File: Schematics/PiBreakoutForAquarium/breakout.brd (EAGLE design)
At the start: 57.1 x 87.3 mm, 17 parts, among them U1 MSP430G2402IN20

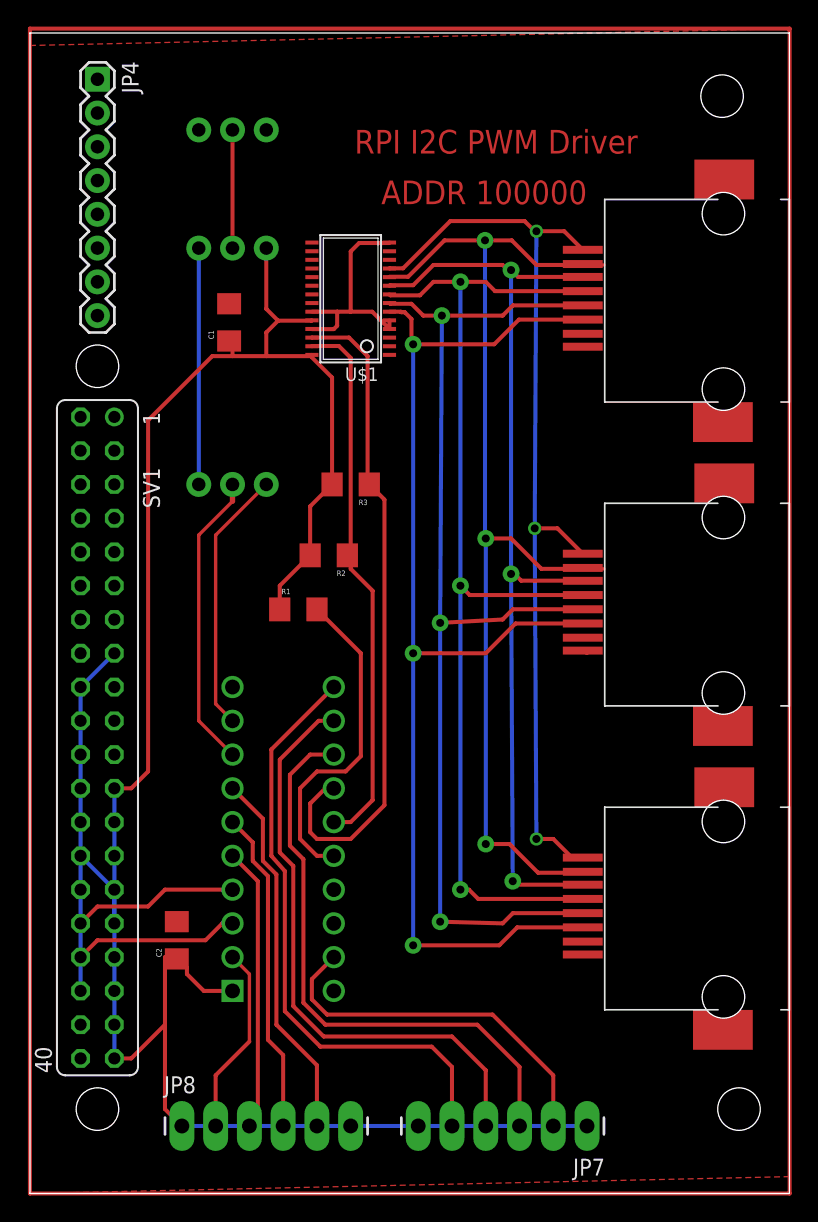
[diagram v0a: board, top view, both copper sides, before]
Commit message: New AVR based firmware
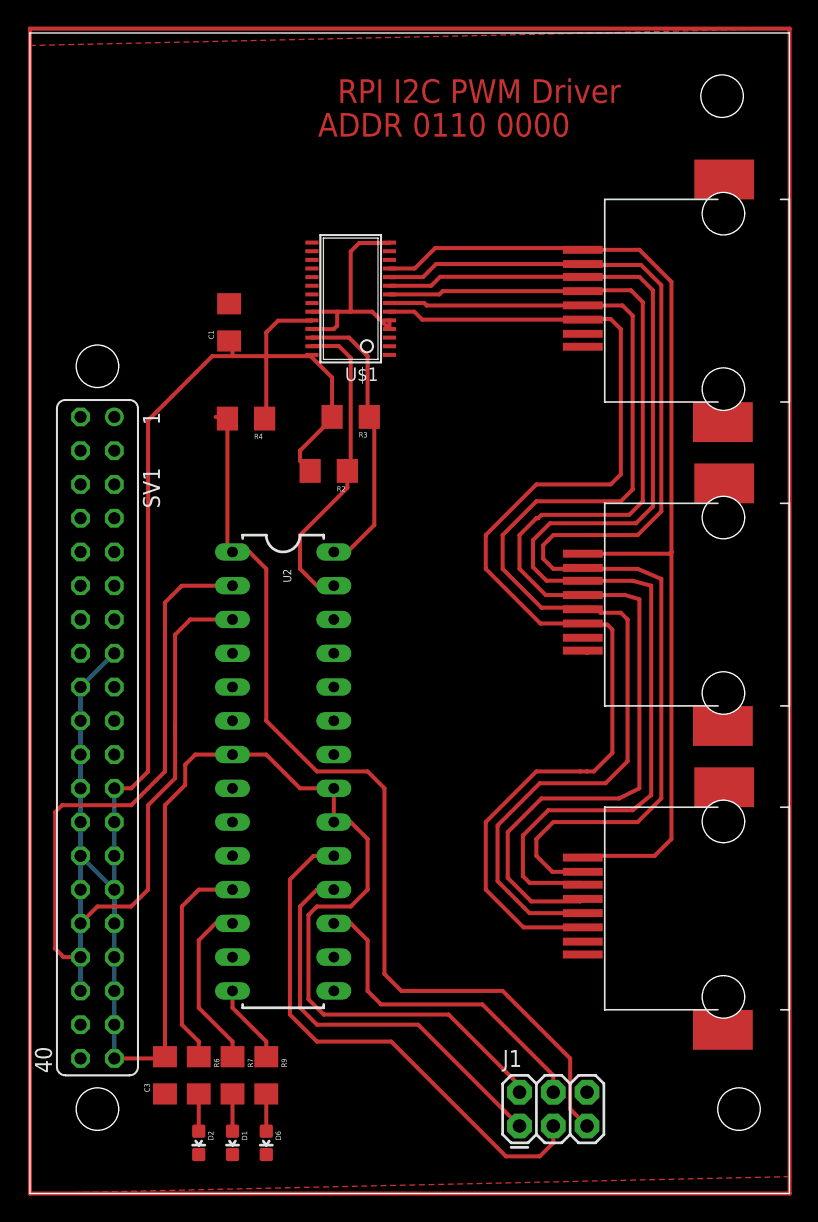
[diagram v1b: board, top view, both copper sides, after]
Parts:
- removed C2: .1 uF, SparkFun-Capacitors:1206
- removed JP2, JP3, JP5: (no value), SparkFun-Connectors:1X03
- removed JP4: (no value), SparkFun-Connectors:1X08
- removed JP7, JP8: (no value), SparkFun-Connectors:1X06_LONGPADS
- removed R1: 47K, SparkFun-Resistors:1206
- removed U1: MSP430G2402IN20, Texas Instruments_By_element14_Batch_1:DIP254P762X508-20
- added C3: (no value), SparkFun-Capacitors:1206
- added D1, D2, D6: (no value), SparkFun-LED:LED-0603
- added J1: FEMALE 2x3, SparkFun-Connectors:2X3
- added R4, R6, R7, R9: (no value), SparkFun-Resistors:1206
- added U2: ATMEGA328P_PDIP, SparkFun-DigitalIC:DIL28-3
- moved R2 6.35 mm to (21.2, 51.8)
- moved R3 5.08 mm to (22.9, 55.9)
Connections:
- removed net N$19: JP7.3, U1.13
- removed net N$22: JP8.3, U1.5
- removed net N$5: R3.1, U$1.26, U1.14
- removed net N$6: R1.2, U1.16
- new net N$16: J1.1, U2.18
- new net N$25: R3.1, U$1.26, U2.28
- net GND: now also C3.1, D1.C, D2.C, D6.C, J1.6, U2.22, U2.8; no longer C2.2, JP2.3, JP3.3, JP5.1, JP7.6, JP8.6, U1.20
- net N$1: now also U2.3; no longer U1.4
- net N$10: now also U2.2; no longer U1.3
- net N$17: now also J1.3, U2.19; no longer JP7.5, U1.11
- net N$18: now also D1.A, R7.2; no longer JP7.4, U1.12
- net N$2: now also J1.5, R4.2, U2.1; no longer JP2.1, U1.9
- net N$20: now also D6.A, R9.2; no longer JP7.2, U1.19
- net N$21: now also R9.1, U2.14; no longer JP8.2, U1.2
- net N$23: now also R7.1, U2.12; no longer JP8.4, U1.6
- net N$24: now also R6.1, U2.11; no longer JP8.5, U1.7
- net N$4: now also U2.27; no longer U1.15
- net N$7: now also D2.A, R6.2; no longer JP3.2, JP5.2
- net N$8: now also J1.4, U2.17; no longer JP2.2, U1.8
- net VDD: now also C3.2, J1.2, R4.1, U2.20, U2.21, U2.7; no longer C2.1, JP3.1, JP7.1, JP8.1, R1.1, U1.1
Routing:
- net N$2: track 19.9 -> 72.8 mm
- net N$5: track 50.3 -> 0.00 mm
- net N$19: track 44.2 -> 0.00 mm
- net N$18: track 44.9 -> 2.80 mm
- net N$16: track 0.00 -> 30.9 mm
- net N$10: track 12.5 -> 40.3 mm
- net N$20: track 28.2 -> 2.80 mm
- net N$6: track 24.9 -> 0.00 mm
- net N$22: track 21.6 -> 0.00 mm
- net N$25: track 0.00 -> 21.6 mm
- net N$14: track 72.7 -> 92.9 mm, vias 3 -> 0
- net N$1: track 12.5 -> 30.9 mm
- net GND: track 69.0 -> 51.2 mm
- net N$4: track 40.7 -> 23.8 mm
- net N$15: track 80.0 -> 92.5 mm, vias 3 -> 0
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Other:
- board text added: "ADDR 0110 0000"
- board text removed: "ADDR 100000"
